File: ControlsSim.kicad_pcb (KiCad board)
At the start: 2 copper layers, 100 x 100 mm, 24 parts, among them J2 Accelerator Pot, J3 Brake Button, J5 Motor Contactors, J6 Array Contactors, J7 Rotary Switch, SW2 SW_Rotary2x6

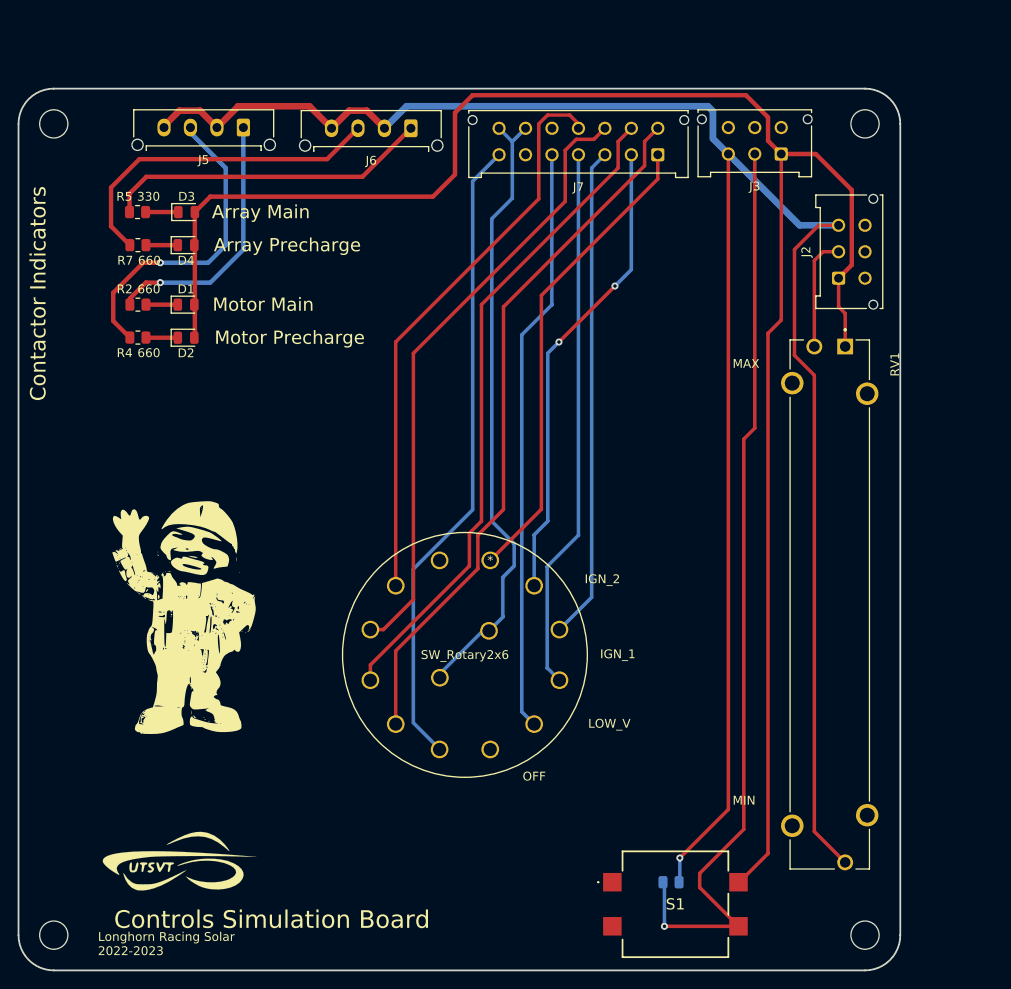
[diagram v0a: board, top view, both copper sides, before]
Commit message: Redesigned the layout to better accomodate the new rotary encoder footprint
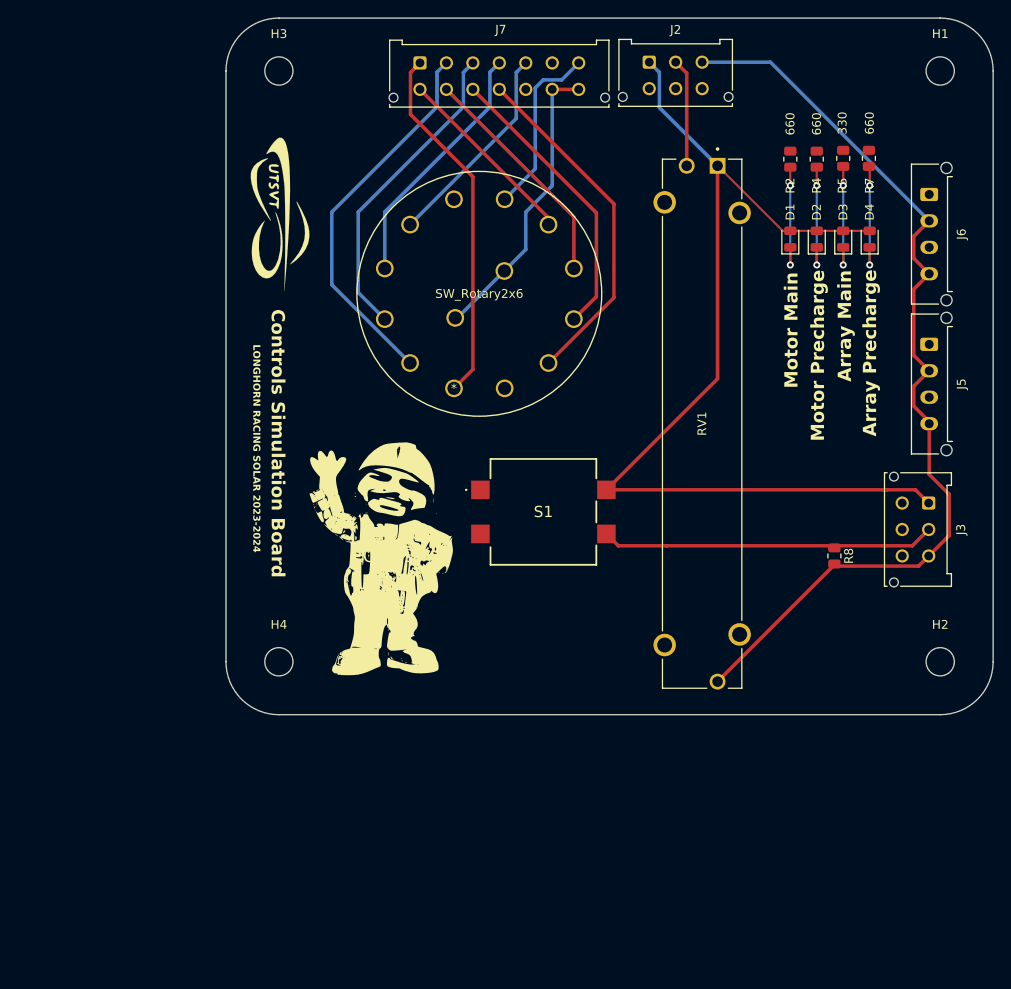
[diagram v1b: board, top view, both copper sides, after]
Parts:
- R8: moved to F.Cu
- moved H1 140.4 mm to (204.5, 48.0)
- moved H3 118.4 mm to (129.5, 48.0)
- moved R7 83.5 mm to (196.4, 57.9), turned to 90 degrees
- moved J5 81.6 mm to (203.3, 79.0), turned to -90 degrees
- moved R5 80.3 mm to (193.5, 57.9), turned to 90 degrees
- moved R4 79.6 mm to (190.5, 58.0), turned to -90 degrees
- moved D4 77.5 mm to (196.5, 67.1), turned to 90 degrees
- moved R2 75.8 mm to (187.5, 58.0), turned to 90 degrees
- moved LOGO2 74.6 mm to (129.5, 64.0), turned to -90 degrees
- moved D3 74.5 mm to (193.5, 67.1), turned to 90 degrees
- moved D2 72.4 mm to (190.5, 67.1), turned to 90 degrees
- moved D1 68.9 mm to (187.5, 67.1), turned to 90 degrees
- moved H4 66.1 mm to (129.5, 115.0)
- moved H2 61.6 mm to (204.5, 115.0)
- moved J6 59.3 mm to (203.3, 62.0), turned to -90 degrees
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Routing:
- net GND: track 253.2 -> 107.3 mm, vias 1 -> 0
- net +3V3: track 207.7 -> 114.4 mm
- net Brk_Signal: track 105.5 -> 37.9 mm, vias 1 -> 0
- net /Rot8: track 79.9 -> 21.4 mm
- net /Rot7: track 72.7 -> 20.2 mm
- net /Rot9: track 74.9 -> 26.3 mm
- net /Rot5: track 66.6 -> 23.8 mm
- net /A_D_Pre2: track 38.2 -> 0.00 mm
- net /RotV+: track 71.0 -> 33.6 mm
- net /Rot10: track 69.9 -> 32.9 mm
- net /A_D_Mn2: track 37.1 -> 0.25 mm
- net /M_D_Pre2: track 35.8 -> 0.00 mm, vias 1 -> 0
- net /Rot4: track 61.6 -> 28.7 mm
- net /M_D_Mn2: track 29.7 -> 0.00 mm, vias 1 -> 0
- net /Rot11: track 64.9 -> 39.5 mm
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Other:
- board size 100 x 100 mm -> 87 x 79 mm
- board text added: "LONGHORN RACING SOLAR 2023-2024"
- board text removed: "Alex Zhang"
- board text removed: "Contactor Indicators"
- board text removed: "IGN_1"
- board text removed: "IGN_2"
- board text removed: "Jacob Pustilnik Lauren Oliveira Aditi Sarlashkar"
- board text removed: "LOW_V"
- board text removed: "Longhorn Racing Solar 2022-2023"
- board text removed: "MAX"
- board text removed: "MIN"
- board text removed: "OFF"

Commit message: Fixed a few errors with the edge cuts (oopsies)
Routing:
- net /M_D_Mn2: track 0.00 -> 40.7 mm
- net /M_D_Pre2: track 0.00 -> 33.2 mm, vias 0 -> 1
- net /A_D_Pre2: track 0.00 -> 18.1 mm
- net /A_D_Mn2: track 0.25 -> 12.1 mm
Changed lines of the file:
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@@
         (effects (font (size 1 1) (thickness 0.15)))
     )
-    (fp_text value "MountingHole" (at 0 4.2) (layer "F.Fab")
+    (fp_text value "MountingHole" (at 0 4.2) (layer "F.Fab") hide
         (effects (font (size 1 1) (thickness 0.15)))
     )
@@
         (effects (font (size 1 1) (thickness 0.15)))
     )
-    (fp_text value "MountingHole" (at 0 4.2) (layer "F.Fab")
+    (fp_text value "MountingHole" (at 0 4.2) (layer "F.Fab") hide
         (effects (font (size 1 1) (thickness 0.15)))
     )
@@
         (effects (font (size 1 1) (thickness 0.15)))
     )
-    (fp_text value "MountingHole" (at 0 4.2) (layer "F.Fab")
+    (fp_text value "MountingHole" (at 0 4.2) (layer "F.Fab") hide
         (effects (font (size 1 1) (thickness 0.15)))
     )
@@
         (effects (font (size 1 1) (thickness 0.15)))
     )
-    (fp_text value "MountingHole" (at 0 4.2) (layer "F.Fab")
+    (fp_text value "MountingHole" (at 0 4.2) (layer "F.Fab") hide
         (effects (font (size 1 1) (thickness 0.15)))
     )
@@
     (effects (font (size 1.5 1.5) (thickness 0.3) bold) (justify left bottom))
   )
-  (dimension (type aligned) (layer "Edge.Cuts")
+  (dimension (type aligned) (layer "User.1")
     (pts (xy 210.528 111) (xy 123.528 111))
     (height 80.999999)
-    (gr_text "87.0000 mm" (at 167.028 28.850001) (layer "Edge.Cuts")
+    (gr_text "87.0000 mm" (at 167.028 28.850001) (layer "User.1")
       (effects (font (size 1 1) (thickness 0.15)))
     )
@@
     (style (thickness 0.1) (arrow_length 1.27) (text_position_mode 0) (extension_height 0.58642) (extension_offset 0.5) keep_text_aligned)
   )
-  (dimension (type aligned) (layer "Edge.Cuts")
-    (pts (xy 192.528 42) (xy 192.528 121))
+  (dimension (type aligned) (layer "User.1")
+    (pts (xy 183.528 42) (xy 183.528 121))
     (height -39)
-    (gr_text "79.0000 mm" (at 230.378 81.5 90) (layer "Edge.Cuts")
+    (gr_text "79.0000 mm" (at 221.378 81.5 90) (layer "User.1")
       (effects (font (size 1 1) (thickness 0.15)))
     )
@@
   (segment (start 171.528 47) (end 172.678 48.15) (width 0.4) (layer "B.Cu") (net 8))
   (segment (start 172.678 52.15) (end 179.278 58.75) (width 0.4) (layer "B.Cu") (net 8))
+  (segment (start 194.3655 57.8375) (end 199.1155 57.8375) (width 0.25) (layer "F.Cu") (net 9))
+  (segment (start 199.1155 57.8375) (end 203.278 62) (width 0.25) (layer "F.Cu") (net 9))
   (segment (start 203.278 62) (end 203.278 62.25) (width 0.4) (layer "F.Cu") (net 9))
-  (segment (start 144.453 52.925) (end 151.528 60) (width 0.4) (layer "F.Cu") (net 10))
+  (segment (start 193.528 57) (end 194.3655 57.8375) (width 0.25) (layer "F.Cu") (net 9))
+  (segment (start 144.378 48.235) (end 144.378 52.85) (width 0.4) (layer "F.Cu") (net 10))
   (segment (start 151.528 60) (end 151.528 81.848745) (width 0.4) (layer "F.Cu") (net 10))
-  (segment (start 145.528 47.085) (end 144.453 48.16) (width 0.4) (layer "F.Cu") (net 10))
   (segment (start 151.528 81.848745) (end 149.385159 83.991586) (width 0.4) (layer "F.Cu") (net 10))
-  (segment (start 144.453 48.16) (end 144.453 52.925) (width 0.4) (layer "F.Cu") (net 10))
-  (segment (start 148.528 47.085) (end 147.453 48.16) (width 0.4) (layer "B.Cu") (net 11))
+  (segment (start 144.378 52.85) (end 151.528 60) (width 0.4) (layer "F.Cu") (net 10))
+  (segment (start 145.528 47.085) (end 144.378 48.235) (width 0.4) (layer "F.Cu") (net 10))
   (segment (start 135.528 64) (end 135.528 72.237494) (width 0.4) (layer "B.Cu") (net 11))
-  (segment (start 147.453 52.075) (end 135.528 64) (width 0.4) (layer "B.Cu") (net 11))
-  (segment (start 147.453 48.16) (end 147.453 52.075) (width 0.4) (layer "B.Cu") (net 11))
+  (segment (start 148.528 47.085) (end 146.678 48.935) (width 0.4) (layer "B.Cu") (net 11))
+  (segment (start 146.678 48.935) (end 146.678 52.85) (width 0.4) (layer "B.Cu") (net 11))
   (segment (start 135.528 72.237494) (end 144.409253 81.118747) (width 0.4) (layer "B.Cu") (net 11))
-  (segment (start 150.453 48.16) (end 150.453 52.075) (width 0.4) (layer "B.Cu") (net 12))
-  (segment (start 151.528 47.085) (end 150.453 48.16) (width 0.4) (layer "B.Cu") (net 12))
+  (segment (start 146.678 52.85) (end 135.528 64) (width 0.4) (layer "B.Cu") (net 11))
   (segment (start 138.528 73.134428) (end 141.536414 76.142842) (width 0.4) (layer "B.Cu") (net 12))
   (segment (start 138.528 64) (end 138.528 73.134428) (width 0.4) (layer "B.Cu") (net 12))
-  (segment (start 150.453 52.075) (end 138.528 64) (width 0.4) (layer "B.Cu") (net 12))
-  (segment (start 153.453 48.16) (end 153.453 52.075) (width 0.4) (layer "B.Cu") (net 13))
-  (segment (start 153.453 52.075) (end 141.536414 63.991586) (width 0.4) (layer "B.Cu") (net 13))
+  (segment (start 151.528 47.085) (end 150.378 48.235) (width 0.4) (layer "B.Cu") (net 12))
+  (segment (start 150.378 52.15) (end 138.528 64) (width 0.4) (layer "B.Cu") (net 12))
+  (segment (start 150.378 48.235) (end 150.378 52.15) (width 0.4) (layer "B.Cu") (net 12))
+  (segment (start 154.528 47.085) (end 153.378 48.235) (width 0.4) (layer "B.Cu") (net 13))
+  (segment (start 153.378 52.15) (end 141.536414 63.991586) (width 0.4) (layer "B.Cu") (net 13))
+  (segment (start 153.378 48.235) (end 153.378 52.15) (width 0.4) (layer "B.Cu") (net 13))
   (segment (start 141.536414 63.991586) (end 141.536414 70.397163) (width 0.4) (layer "B.Cu") (net 13))
-  (segment (start 154.528 47.085) (end 153.453 48.16) (width 0.4) (layer "B.Cu") (net 13))
-  (segment (start 157.528 47.085) (end 156.453 48.16) (width 0.4) (layer "B.Cu") (net 14))
-  (segment (start 156.453 53.377511) (end 144.409253 65.421258) (width 0.4) (layer "B.Cu") (net 14))
-  (segment (start 156.453 48.16) (end 156.453 53.377511) (width 0.4) (layer "B.Cu") (net 14))
-  (segment (start 159.518 49.01) (end 158.603 49.925) (width 0.4) (layer "B.Cu") (net 15))
-  (segment (start 161.603 49.01) (end 159.518 49.01) (width 0.4) (layer "B.Cu") (net 15))
-  (segment (start 163.528 47.085) (end 161.603 49.01) (width 0.4) (layer "B.Cu") (net 15))
-  (segment (start 158.603 59.076256) (end 155.130837 62.548419) (width 0.4) (layer "B.Cu") (net 15))
-  (segment (start 158.603 49.925) (end 158.603 59.076256) (width 0.4) (layer "B.Cu") (net 15))
+  (segment (start 157.528 47.085) (end 156.378 48.235) (width 0.4) (layer "B.Cu") (net 14))
+  (segment (start 156.378 48.235) (end 156.378 53.452511) (width 0.4) (layer "B.Cu") (net 14))
+  (segment (start 156.378 53.452511) (end 144.409253 65.421258) (width 0.4) (layer "B.Cu") (net 14))
+  (segment (start 160.293 48.235) (end 159.378 49.15) (width 0.4) (layer "B.Cu") (net 15))
+  (segment (start 159.378 58.301256) (end 155.130837 62.548419) (width 0.4) (layer "B.Cu") (net 15))
+  (segment (start 159.378 49.15) (end 159.378 58.301256) (width 0.4) (layer "B.Cu") (net 15))
+  (segment (start 163.528 47.085) (end 162.378 48.235) (width 0.4) (layer "B.Cu") (net 15))
+  (segment (start 162.378 48.235) (end 160.293 48.235) (width 0.4) (layer "B.Cu") (net 15))
   (segment (start 160.106742 64.663742) (end 160.106742 65.421258) (width 0.4) (layer "F.Cu") (net 16))
   (segment (start 145.528 50.085) (end 160.106742 64.663742) (width 0.4) (layer "F.Cu") (net 16))
@@
   (segment (start 203.218 100) (end 201.368 101.85) (width 0.4) (layer "F.Cu") (net 25))
   (segment (start 168.028 101.85) (end 166.678 100.5) (width 0.4) (layer "F.Cu") (net 25))
+  (segment (start 191.553 61.025) (end 192.528 62) (width 0.25) (layer "F.Cu") (net 33))
+  (segment (start 191.553 58.1125) (end 191.553 61.025) (width 0.25) (layer "F.Cu") (net 33))
+  (segment (start 190.528 57.0875) (end 191.553 58.1125) (width 0.25) (layer "F.Cu") (net 33))
+  (via (at 192.528 62) (size 0.8) (drill 0.4) (layers "F.Cu" "B.Cu") (net 33))
+  (segment (start 192.528 74.25) (end 203.278 85) (width 0.25) (layer "B.Cu") (net 33))
+  (segment (start 192.528 62) (end 192.528 74.25) (width 0.25) (layer "B.Cu") (net 33))
+  (segment (start 188.453 56.1625) (end 200.326896 56.1625) (width 0.25) (layer "F.Cu") (net 34))
+  (segment (start 187.528 57.0875) (end 188.453 56.1625) (width 0.25) (layer "F.Cu") (net 34))
+  (segment (start 204.528 79) (end 203.278 79) (width 0.25) (layer "F.Cu") (net 34))
+  (segment (start 200.326896 56.1625) (end 206.528 62.363604) (width 0.25) (layer "F.Cu") (net 34))
+  (segment (start 206.528 77) (end 204.528 79) (width 0.25) (layer "F.Cu") (net 34))
+  (segment (start 206.528 62.363604) (end 206.528 77) (width 0.25) (layer "F.Cu") (net 34))
+  (segment (start 196.4405 57) (end 200.528 57) (width 0.25) (layer "F.Cu") (net 35))
+  (segment (start 205.528 62) (end 205.528 65.75) (width 0.25) (layer "F.Cu") (net 35))
+  (segment (start 200.528 57) (end 205.528 62) (width 0.25) (layer "F.Cu") (net 35))
+  (segment (start 205.528 65.75) (end 203.278 68) (width 0.25) (layer "F.Cu") (net 35))
 )
